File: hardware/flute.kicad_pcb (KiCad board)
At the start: 2 copper layers, 230 x 20 mm, 34 parts, among them J1 Conn_01x04, J4 Conn_01x02, SW1 C, SW2 D, SW3 E, SW4 F, SW5 G, SW6 A, SW7 H, SW8 OCTAVE?, U1 W25Q128JVS, Y1 Crystal_GND24

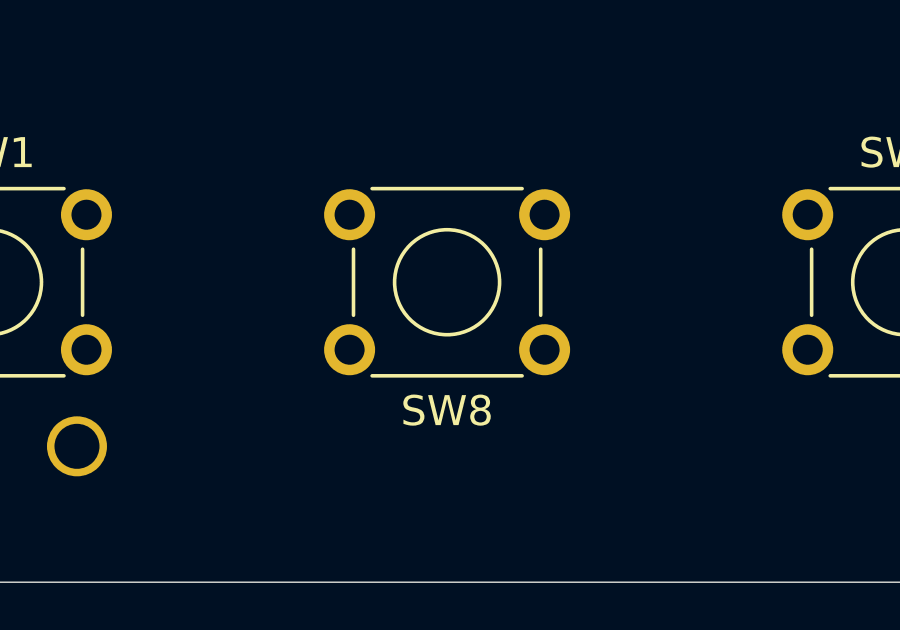
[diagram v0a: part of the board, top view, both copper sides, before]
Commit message: OCTAVE button moved to the pcb bottom
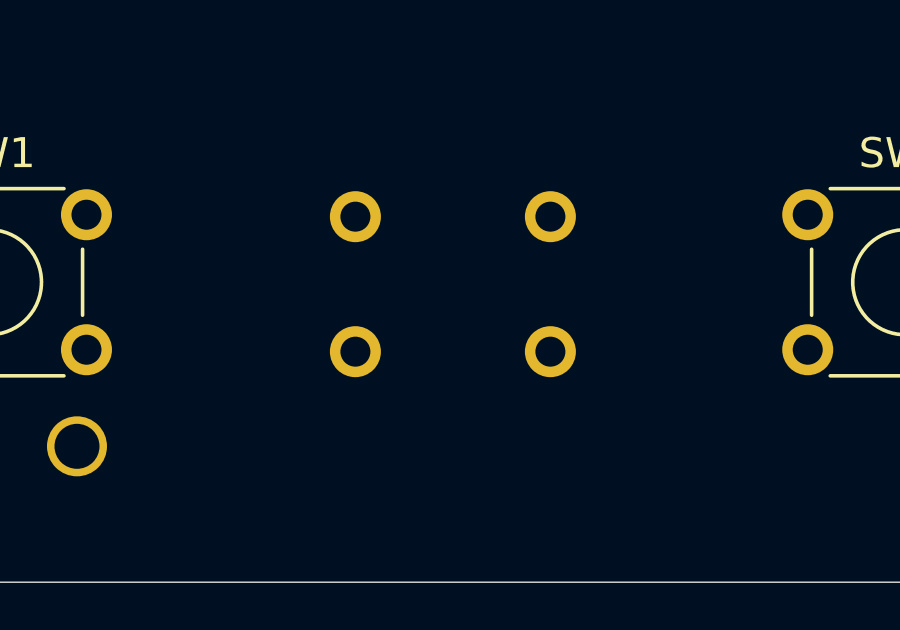
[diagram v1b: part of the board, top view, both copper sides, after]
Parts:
- SW8: moved to B.Cu
- moved SW8 4.44 mm to (124.7, 128.2)

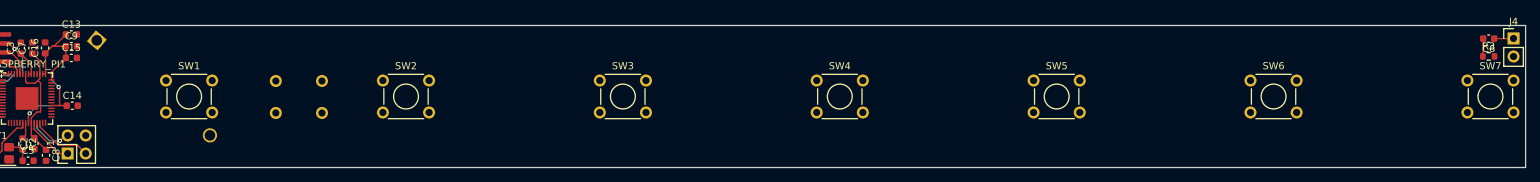
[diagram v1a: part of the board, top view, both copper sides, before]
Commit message: buttons added to the pcb
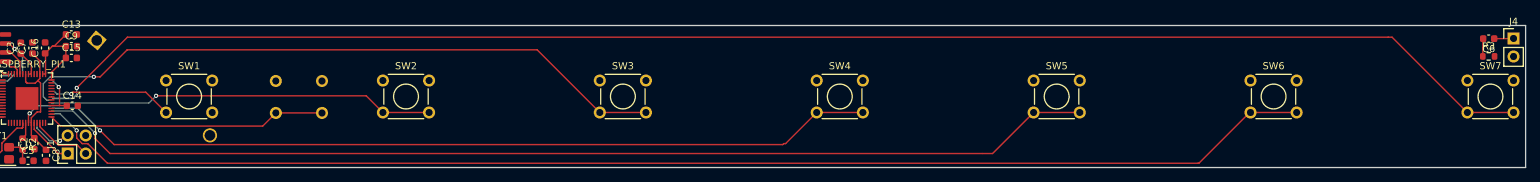
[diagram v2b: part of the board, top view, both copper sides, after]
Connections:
- SW1 pad 2: GPIO2 -> GPIO26
- SW2 pad 2: GPIO3 -> GPIO22
- SW3 pad 2: GPIO4 -> GPIO23
- SW4 pad 2: GPIO5 -> GPIO21
- SW5 pad 2: GPIO6 -> GPIO20
- SW6 pad 2: GPIO7 -> GPIO19
- SW7 pad 2: GPIO8 -> GPIO24
- SW8 pad 2: GPIO9 -> GPIO18
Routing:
- net GPIO24: track 0.00 -> 218.7 mm, vias 0 -> 1
- net GPIO19: track 0.00 -> 181.8 mm, vias 0 -> 1
- net GPIO20: track 0.00 -> 150.1 mm, vias 0 -> 1
- net GPIO21: track 0.00 -> 118.2 mm, vias 0 -> 1
- net GPIO23: track 0.00 -> 93.6 mm, vias 0 -> 1
- net GPIO22: track 0.00 -> 54.6 mm, vias 0 -> 1
- net GPIO18: track 0.00 -> 39.4 mm
- net GPIO26: track 0.00 -> 17.2 mm, vias 0 -> 1

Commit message: pcb connections corrected
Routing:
- net GPIO24: track 218.7 -> 214.2 mm, vias 1 -> 2
- net GPIO21: track 118.2 -> 120.3 mm, vias 1 -> 2
- net /RASPBERRY_PI_PICO/SWDIO: track 6.11 -> 7.98 mm, vias 1 -> 2
- net /RASPBERRY_PI_PICO/QSPI_SD2: track 10.5 -> 12.0 mm, vias 1 -> 2
- net +3V3: track 37.0 -> 38.4 mm, vias 2 -> 3
- net /RASPBERRY_PI_PICO/QSPI_SD1: track 9.99 -> 11.0 mm, vias 1 -> 2
- net /RASPBERRY_PI_PICO/QSPI_SD3: track 5.62 -> 5.99 mm, vias 1 -> 2
- net GPIO20: track 150.1 -> 150.4 mm, vias 1 -> 2
- net GPIO26: track 17.2 -> 17.4 mm, vias 1 -> 0
- net GPIO23: track 93.6 -> 93.8 mm, vias 1 -> 3
- net GPIO22: track 54.6 -> 54.5 mm, vias 1 -> 2
- net GPIO19: vias 1 -> 2

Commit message: zonefills for pcb
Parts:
- moved C3 47.7 mm to (128.8, 134.5)
- moved R1 46.3 mm to (113.8, 141.2), turned to 90 degrees
- moved C13 46.3 mm to (133.9, 134.4)
- moved C9 46.2 mm to (133.8, 136.1)
- moved C15 46.2 mm to (133.8, 137.8)
- moved C16 46.1 mm to (130.5, 134.5)
- moved C1 46.0 mm to (112.0, 141.3)
- moved SW5 45.8 mm to (269.4, 139.2)
- moved BT1 45.8 mm to (137.5, 133.5)
- moved C10 45.8 mm to (120.4, 140.9)
- moved C11 45.8 mm to (120.4, 139.1)
- moved C12 45.8 mm to (120.5, 142.7)
- moved C14 45.8 mm to (134.0, 142.7)
- moved C6 45.8 mm to (333.5, 133.2)
- moved J1 45.8 mm to (133.4, 149.4)
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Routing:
- net +3V3: track 38.4 -> 69.3 mm, vias 3 -> 4
- net GPIO22: track 54.5 -> 40.8 mm, vias 2 -> 0
- net GPIO23: track 93.8 -> 82.1 mm, vias 3 -> 0
- net GPIO21: track 120.3 -> 108.7 mm, vias 2 -> 0
- net GPIO25: track 0.00 -> 7.41 mm
- net GPIO27: track 0.00 -> 7.12 mm
- net GPIO24: track 214.2 -> 207.3 mm, vias 2 -> 0
- net GND: track 0.00 -> 6.72 mm, vias 0 -> 8
- net GPIO28: track 0.00 -> 5.77 mm
- net +1V1: track 19.1 -> 16.1 mm
- net GPIO26: track 17.4 -> 19.7 mm
- net GPIO18: track 39.4 -> 41.5 mm
- net GPIO19: track 181.8 -> 179.8 mm, vias 2 -> 0
- net /RASPBERRY_PI_PICO/RUN: track 8.56 -> 10.4 mm
- net GPIO20: track 150.4 -> 148.7 mm, vias 2 -> 0
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- added copper zone on B.Cu, net GND
- added copper zone on F.Cu, net GND

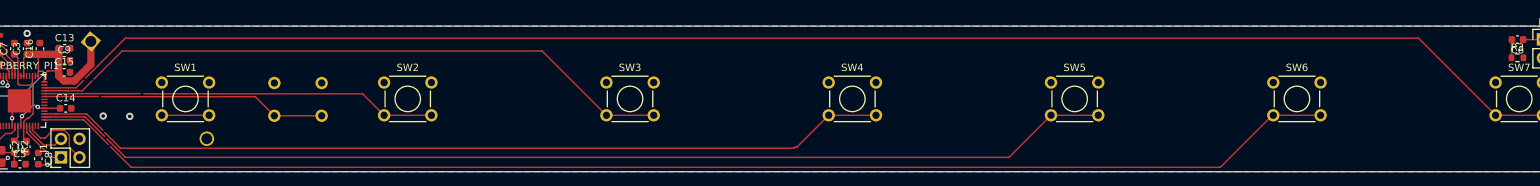
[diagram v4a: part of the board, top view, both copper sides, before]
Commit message: type of connections changed
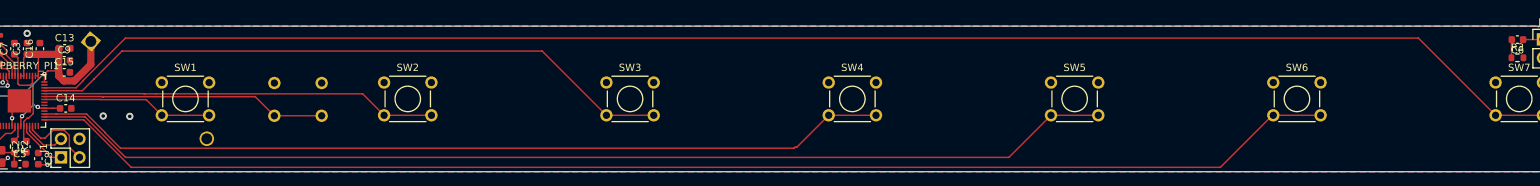
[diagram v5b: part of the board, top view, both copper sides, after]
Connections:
- net GPIO0 renamed /RASPBERRY_PI_PICO/GPIO0
- net GPIO1 renamed /RASPBERRY_PI_PICO/GPIO1
- net GPIO10 renamed /RASPBERRY_PI_PICO/GPIO10
- net GPIO11 renamed /MICROPHONE/GPIO11
- net GPIO12 renamed /RASPBERRY_PI_PICO/GPIO12
- net GPIO13 renamed /RASPBERRY_PI_PICO/GPIO13
- net GPIO14 renamed /RASPBERRY_PI_PICO/GPIO14
- net GPIO15 renamed /RASPBERRY_PI_PICO/GPIO15
- net GPIO16 renamed /RASPBERRY_PI_PICO/GPIO16
- net GPIO17 renamed /RASPBERRY_PI_PICO/GPIO17
- net GPIO2 renamed /RASPBERRY_PI_PICO/GPIO2
- net GPIO29 renamed /RASPBERRY_PI_PICO/PWM_OUT
- net GPIO3 renamed /RASPBERRY_PI_PICO/GPIO3
- net GPIO4 renamed /RASPBERRY_PI_PICO/GPIO4
- net GPIO5 renamed /RASPBERRY_PI_PICO/GPIO5
- net GPIO6 renamed /RASPBERRY_PI_PICO/GPIO6
- net GPIO7 renamed /RASPBERRY_PI_PICO/GPIO7
- net GPIO8 renamed /RASPBERRY_PI_PICO/GPIO8
- net GPIO9 renamed /RASPBERRY_PI_PICO/GPIO9
- RASPBERRY_PI1 pad 29: GPIO18 -> /BUTTONS/KEY_A
- RASPBERRY_PI1 pad 30: GPIO19 -> /BUTTONS/KEY_G
- RASPBERRY_PI1 pad 31: GPIO20 -> /BUTTONS/KEY_F
- RASPBERRY_PI1 pad 32: GPIO21 -> /RASPBERRY_PI_PICO/GPIO21
- RASPBERRY_PI1 pad 34: GPIO22 -> /RASPBERRY_PI_PICO/GPIO22
- RASPBERRY_PI1 pad 35: GPIO23 -> /RASPBERRY_PI_PICO/GPIO23
- RASPBERRY_PI1 pad 36: GPIO24 -> /BUTTONS/KEY_C
- RASPBERRY_PI1 pad 37: GPIO25 -> /BUTTONS/KEY_OCTAVE
- RASPBERRY_PI1 pad 38: GPIO26 -> /BUTTONS/KEY_D
- RASPBERRY_PI1 pad 39: GPIO27 -> /BUTTONS/KEY_E
- RASPBERRY_PI1 pad 40: GPIO28 -> /BUTTONS/KEY_H
- SW1 pad 2: GPIO26 -> /BUTTONS/KEY_C
- SW2 pad 2: GPIO22 -> /BUTTONS/KEY_D
- SW3 pad 2: GPIO23 -> /BUTTONS/KEY_E
- SW4 pad 2: GPIO21 -> /BUTTONS/KEY_F
- SW5 pad 2: GPIO20 -> /BUTTONS/KEY_G
- SW6 pad 2: GPIO19 -> /BUTTONS/KEY_A
- SW7 pad 2: GPIO24 -> /BUTTONS/KEY_H
- SW8 pad 2: GPIO18 -> /BUTTONS/KEY_OCTAVE
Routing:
- net /BUTTONS/KEY_H: track 0.00 -> 213.4 mm
- net GPIO24: track 207.3 -> 0.00 mm
- net /BUTTONS/KEY_A: track 0.00 -> 181.0 mm
- net GPIO19: track 179.8 -> 0.00 mm
- net /BUTTONS/KEY_G: track 0.00 -> 149.5 mm
- net GPIO20: track 148.7 -> 0.00 mm
- net /BUTTONS/KEY_F: track 0.00 -> 118.2 mm
- net GPIO21: track 108.7 -> 0.00 mm
- net /BUTTONS/KEY_E: track 0.00 -> 89.6 mm
- net GPIO23: track 82.1 -> 0.00 mm
- net /BUTTONS/KEY_D: track 0.00 -> 54.6 mm
- net GPIO18: track 41.5 -> 0.00 mm
- net GPIO22: track 40.8 -> 0.00 mm
- net /BUTTONS/KEY_OCTAVE: track 0.00 -> 39.4 mm
- net /BUTTONS/KEY_C: track 0.00 -> 23.5 mm
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
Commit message: complete pcb ver1
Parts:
- removed the C1 at (112.0, 141.3)
- removed the R1 at (113.8, 141.2)
- added C2: 1uF, Capacitor_SMD:C_0603_1608Metric, F.Cu at (38.8, 111.2)
- added R2: 2.2K, Resistor_SMD:R_0603_1608Metric, F.Cu at (37.0, 111.3)
- moved J3 104.4 mm to (39.8, 103.2), turned to 0 degrees
- moved C13 94.7 mm to (45.2, 110.0), turned to 180 degrees
- moved C6 93.6 mm to (49.0, 103.2), turned to 90 degrees
- moved BT1 92.3 mm to (46.2, 119.4), turned to 47 degrees
- moved C14 91.7 mm to (45.2, 114.0), turned to 180 degrees
- moved C7 90.9 mm to (45.2, 115.6), turned to 180 degrees
- moved C11 90.3 mm to (45.2, 117.2), turned to 180 degrees
- moved C5 90.1 mm to (51.5, 102.4), turned to 180 degrees
- moved C12 89.2 mm to (50.6, 104.8), turned to -90 degrees
- moved R3 86.3 mm to (52.2, 104.8), turned to 90 degrees
- moved SW8 85.4 mm to (87.7, 113.7), turned to 0 degrees
- moved C15 83.4 mm to (48.7, 118.2), turned to -90 degrees
- moved Y1 82.7 mm to (55.2, 103.4), turned to 180 degrees
- moved U1 82.1 mm to (51.5, 111.0), turned to 180 degrees
- moved C1 80.8 mm to (258.5, 103.2)
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- renumbered C6 to C1, C12 to C10, C13 to C11, C2 to C12, C14 to C13, C15 to C14, C16 to C15, C3 to C16, C4 to C3, C7 to C4, C8 to C6, C9 to C7, C10 to C8, C11 to C9, J4 to J2, J1 to J3, R3 to R1, R2 to R3, RASPBERRY_PI1 to U1, U1 to U2
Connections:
- net /RASPBERRY_PI_PICO/PWM_OUT renamed /RASPBERRY_PI_PICO/GPIO29
- J3 pad 1: /RASPBERRY_PI_PICO/SWCLK -> /RASPBERRY_PI_PICO/SWDIO
- J3 pad 2: /RASPBERRY_PI_PICO/SWDIO -> /RASPBERRY_PI_PICO/SWCLK
- SW1 pad 2: /BUTTONS/KEY_C -> /KEY_C
- SW2 pad 2: /BUTTONS/KEY_D -> /KEY_D
- SW3 pad 2: /BUTTONS/KEY_E -> /KEY_E
- SW4 pad 2: /BUTTONS/KEY_F -> /KEY_F
- SW5 pad 2: /BUTTONS/KEY_G -> /KEY_G
- SW6 pad 2: /BUTTONS/KEY_A -> /KEY_A
- SW7 pad 2: /BUTTONS/KEY_H -> /KEY_H
- SW8 pad 2: /BUTTONS/KEY_OCTAVE -> /KEY_OCTAVE
- U1 pad 12: /RASPBERRY_PI_PICO/GPIO9 -> /KEY_C
- U1 pad 13: /RASPBERRY_PI_PICO/GPIO10 -> /KEY_OCTAVE
- U1 pad 14: /MICROPHONE/GPIO11 -> /KEY_D
- U1 pad 15: /RASPBERRY_PI_PICO/GPIO12 -> /PWM_OUT
- U1 pad 16: /RASPBERRY_PI_PICO/GPIO13 -> /KEY_E
- U1 pad 17: /RASPBERRY_PI_PICO/GPIO14 -> /KEY_F
- U1 pad 18: /RASPBERRY_PI_PICO/GPIO15 -> /KEY_G
- U1 pad 29: /BUTTONS/KEY_A -> /RASPBERRY_PI_PICO/GPIO18
- U1 pad 30: /BUTTONS/KEY_G -> /RASPBERRY_PI_PICO/GPIO19
- U1 pad 31: /BUTTONS/KEY_F -> /RASPBERRY_PI_PICO/GPIO20
- U1 pad 36: /BUTTONS/KEY_C -> /RASPBERRY_PI_PICO/GPIO24
- U1 pad 37: /BUTTONS/KEY_OCTAVE -> /RASPBERRY_PI_PICO/GPIO25
- U1 pad 38: /BUTTONS/KEY_D -> /MIC_OUTPUT
- U1 pad 39: /BUTTONS/KEY_E -> /RASPBERRY_PI_PICO/GPIO27
- U1 pad 4: /RASPBERRY_PI_PICO/GPIO2 -> /KEY_H
- U1 pad 40: /BUTTONS/KEY_H -> /RASPBERRY_PI_PICO/GPIO28
- U1 pad 8: /RASPBERRY_PI_PICO/GPIO6 -> /KEY_A
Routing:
- net /BUTTONS/KEY_H: track 213.4 -> 0.00 mm
- net /KEY_H: track 0.00 -> 210.4 mm
- net /PWM_OUT: track 2.52 -> 208.2 mm, vias 0 -> 2
- net /BUTTONS/KEY_A: track 181.0 -> 0.00 mm
- net /KEY_A: track 0.00 -> 179.3 mm
- net /KEY_G: track 0.00 -> 150.6 mm
- net /BUTTONS/KEY_G: track 149.5 -> 0.00 mm
- net /KEY_F: track 0.00 -> 119.3 mm
- net /BUTTONS/KEY_F: track 118.2 -> 0.00 mm
- net /BUTTONS/KEY_E: track 89.6 -> 0.00 mm
- net /KEY_E: track 0.00 -> 87.8 mm
- net /KEY_D: track 0.00 -> 55.4 mm
- net /BUTTONS/KEY_D: track 54.6 -> 0.00 mm
- net /KEY_OCTAVE: track 0.00 -> 40.2 mm
- net /BUTTONS/KEY_OCTAVE: track 39.4 -> 0.00 mm
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- added copper zone on F.Cu, net +3V3
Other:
- board text added: "GND"
- board text added: "KN HARDWIRE ELECTRONIC FLUTE VER 1.0 AGH UNIVERSITY OF CRACOW 2025"
- board text added: "RUN"
- board text added: "S_CLK"
- board text added: "S_IO"

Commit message: test points added to the schematic
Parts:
- added TP1: TestPoint, TestPoint:TestPoint_Pad_D1.5mm, F.Cu at (61.6, 114.0)
- added TP10: TestPoint, TestPoint:TestPoint_Pad_D1.5mm, F.Cu at (29.8, 130.3)
- added TP11: TestPoint, TestPoint:TestPoint_Pad_D1.5mm, F.Cu at (63.0, 128.4)
- added TP12: TestPoint, TestPoint:TestPoint_Pad_D1.5mm, F.Cu at (42.5, 96.1)
- added TP13: TestPoint, TestPoint:TestPoint_Pad_D1.5mm, F.Cu at (47.9, 93.9)
- added TP14: TestPoint, TestPoint:TestPoint_Pad_D1.5mm, F.Cu at (37.8, 84.5)
- added TP15: TestPoint, TestPoint:TestPoint_Pad_D1.5mm, F.Cu at (31.0, 116.6)
- added TP16: TestPoint, TestPoint:TestPoint_Pad_D1.5mm, F.Cu at (25.3, 124.2)
- added TP17: TestPoint, TestPoint:TestPoint_Pad_D1.5mm, F.Cu at (70.4, 128.8)
- added TP18: TestPoint, TestPoint:TestPoint_Pad_D1.5mm, F.Cu at (33.4, 96.8)
- added TP19: TestPoint, TestPoint:TestPoint_Pad_D1.5mm, F.Cu at (55.0, 93.1)
- added TP2: TestPoint, TestPoint:TestPoint_Pad_D1.5mm, F.Cu at (56.0, 126.9)
- added TP20: TestPoint, TestPoint:TestPoint_Pad_D1.5mm, F.Cu at (47.9, 84.7)
- added TP21: TestPoint, TestPoint:TestPoint_Pad_D1.5mm, F.Cu at (50.2, 129.5)
- added TP3: TestPoint, TestPoint:TestPoint_Pad_D1.5mm, F.Cu at (41.8, 125.5)
- added TP4: TestPoint, TestPoint:TestPoint_Pad_D1.5mm, F.Cu at (56.0, 130.4)
- added TP5: TestPoint, TestPoint:TestPoint_Pad_D1.5mm, F.Cu at (31.5, 124.8)
- added TP6: TestPoint, TestPoint:TestPoint_Pad_D1.5mm, F.Cu at (78.6, 126.7)
- added TP7: TestPoint, TestPoint:TestPoint_Pad_D1.5mm, F.Cu at (65.4, 96.9)
- added TP8: TestPoint, TestPoint:TestPoint_Pad_D1.5mm, F.Cu at (73.8, 96.4)
- added TP9: TestPoint, TestPoint:TestPoint_Pad_D1.5mm, F.Cu at (57.5, 84.2)
- moved C11 0.85 mm to (58.8, 114.4)
- renumbered C2 to C1, C8 to C10, C9 to C11, C10 to C12, C11 to C13, C13 to C14, C14 to C15, C15 to C16, C1 to C2, C12 to C3, C16 to C4, C3 to C5, C5 to C6, C4 to C7, C6 to C8, C7 to C9, J2 to J1, R2 to R1, R1 to R2
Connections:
- net /RASPBERRY_PI_PICO/GPIO0 renamed Net-(U1-GPIO0)
- U1 pad 11: /RASPBERRY_PI_PICO/GPIO8 -> Net-(U1-GPIO8)
- U1 pad 27: /RASPBERRY_PI_PICO/GPIO16 -> Net-(U1-GPIO16)
- U1 pad 28: /RASPBERRY_PI_PICO/GPIO17 -> Net-(U1-GPIO17)
- U1 pad 29: /RASPBERRY_PI_PICO/GPIO18 -> Net-(U1-GPIO18)
- U1 pad 30: /RASPBERRY_PI_PICO/GPIO19 -> Net-(U1-GPIO19)
- U1 pad 31: /RASPBERRY_PI_PICO/GPIO20 -> Net-(U1-GPIO20)
- U1 pad 32: /RASPBERRY_PI_PICO/GPIO21 -> Net-(U1-GPIO21)
- U1 pad 34: /RASPBERRY_PI_PICO/GPIO22 -> Net-(U1-GPIO22)
- U1 pad 35: /RASPBERRY_PI_PICO/GPIO23 -> Net-(U1-GPIO23)
- U1 pad 36: /RASPBERRY_PI_PICO/GPIO24 -> Net-(U1-GPIO24)
- U1 pad 37: /RASPBERRY_PI_PICO/GPIO25 -> Net-(U1-GPIO25)
- U1 pad 39: /RASPBERRY_PI_PICO/GPIO27 -> Net-(U1-GPIO27_ADC1)
- U1 pad 40: /RASPBERRY_PI_PICO/GPIO28 -> Net-(U1-GPIO28_ADC2)
- U1 pad 41: /RASPBERRY_PI_PICO/GPIO29 -> Net-(U1-GPIO29_ADC3)
- U1 pad 5: /RASPBERRY_PI_PICO/GPIO3 -> Net-(U1-GPIO3)
- U1 pad 6: /RASPBERRY_PI_PICO/GPIO4 -> Net-(U1-GPIO4)
- U1 pad 7: /RASPBERRY_PI_PICO/GPIO5 -> Net-(U1-GPIO5)
- U1 pad 9: /RASPBERRY_PI_PICO/GPIO7 -> Net-(U1-GPIO7)
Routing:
- net Net-(U1-GPIO0): track 0.00 -> 0.54 mm

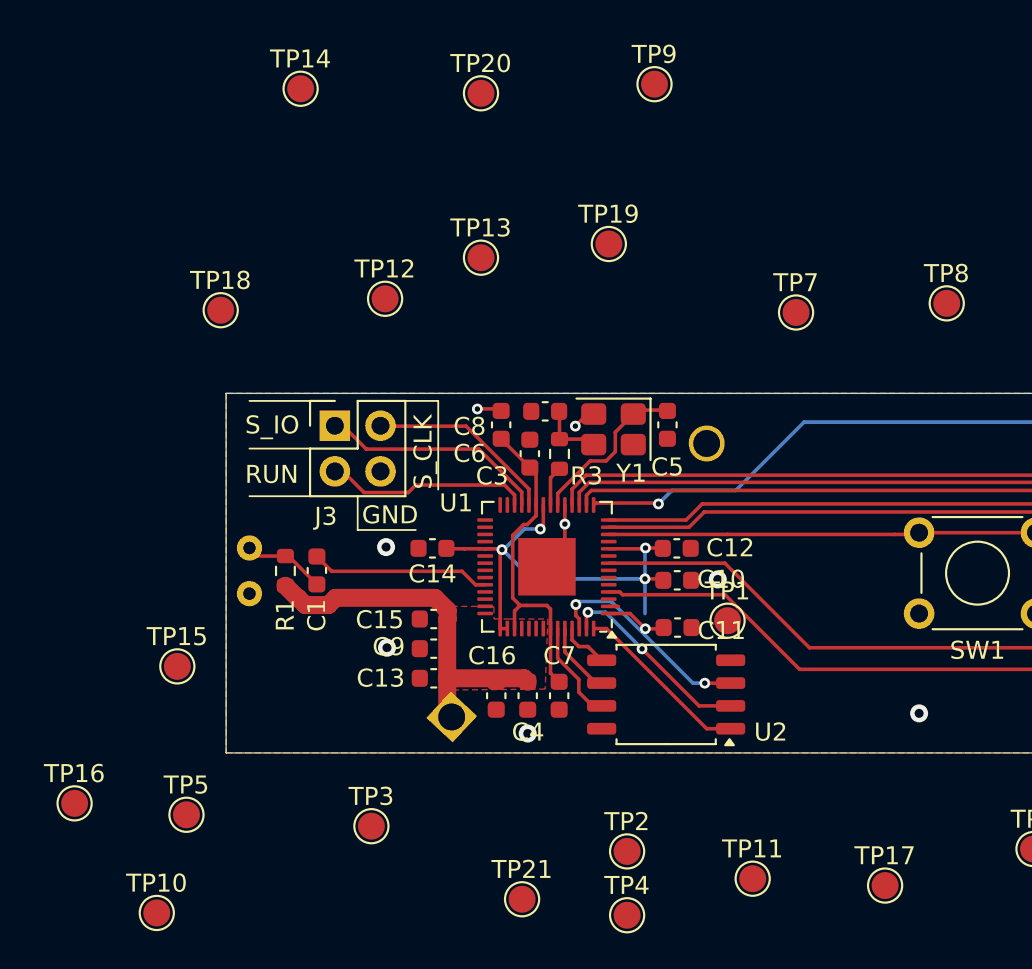
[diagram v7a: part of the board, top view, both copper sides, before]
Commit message: first part of test points placed on pcb
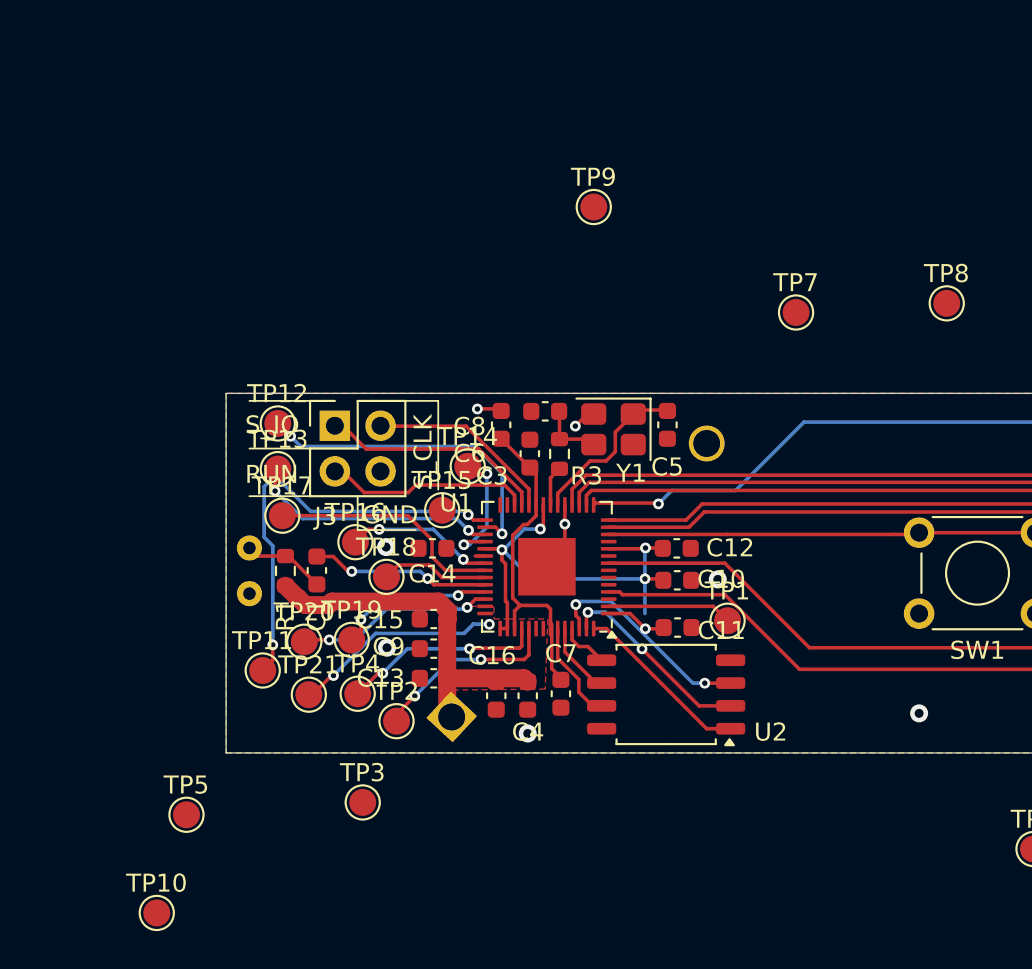
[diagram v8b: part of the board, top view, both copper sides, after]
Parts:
- moved TP17 39.3 mm to (36.8, 108.2)
- moved TP20 32.1 mm to (38.0, 115.2)
- moved TP11 29.6 mm to (35.7, 116.8)
- moved TP19 26.3 mm to (40.7, 115.1)
- moved TP14 23.0 mm to (47.1, 105.5)
- moved TP16 21.3 mm to (40.9, 109.7)
- moved TP4 19.4 mm to (41.0, 118.1)
- moved TP18 17.5 mm to (42.6, 111.6)
- moved TP15 17.1 mm to (45.7, 107.9)
- moved TP21 16.4 mm to (38.3, 118.2)
- moved TP13 16.3 mm to (36.6, 105.6)
- moved TP2 14.7 mm to (43.2, 119.6)
- moved TP12 9.15 mm to (36.6, 103.1)
- moved TP9 7.62 mm to (54.2, 91.0)
- moved TP3 1.41 mm to (41.3, 124.2)
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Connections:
- TP1 pad 2: (no net) -> Net-(U1-GPIO0)
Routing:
- net Net-(U1-GPIO18): track 0.00 -> 24.0 mm, vias 0 -> 2
- net Net-(U1-GPIO19): track 0.00 -> 18.1 mm, vias 0 -> 2
- net Net-(U1-GPIO20): track 0.00 -> 14.0 mm, vias 0 -> 2
- net Net-(U1-GPIO24): track 0.00 -> 13.1 mm
- net Net-(U1-GPIO29_ADC3): track 0.00 -> 11.7 mm, vias 0 -> 2
- net /RASPBERRY_PI_PICO/USB_DM: track 0.00 -> 11.2 mm, vias 0 -> 2
- net Net-(U1-GPIO28_ADC2): track 0.00 -> 11.0 mm, vias 0 -> 2
- net /RASPBERRY_PI_PICO/USB_DP: track 0.00 -> 10.6 mm, vias 0 -> 2
- net Net-(U1-GPIO27_ADC1): track 0.00 -> 8.89 mm, vias 0 -> 2
- net Net-(U1-GPIO23): track 0.00 -> 8.29 mm, vias 0 -> 2
- net Net-(U1-GPIO21): track 0.00 -> 7.15 mm, vias 0 -> 2
- net Net-(U1-GPIO0): track 0.54 -> 6.94 mm
- net Net-(U1-GPIO25): track 0.00 -> 6.05 mm
- net +3V3: track 53.1 -> 51.0 mm
- net Net-(U1-GPIO22): track 0.00 -> 1.06 mm
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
